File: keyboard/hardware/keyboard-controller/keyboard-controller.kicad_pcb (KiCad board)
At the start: 2 copper layers, 195 x 65 mm, 50 parts, among them J1 Debug_Pins, J2 Barrel_Jack_Switch, J3 Keybed Connector, J5 CV_OUT, J6 GATE_OUT, SW3 OCTAVE_UP, SW4 OCTAVE_DOWN, SW5 FUNC, U1 Pico, U2 MCP4921, U3 L78L09_TO92, U4 TL431, U5 LM1117-3.3, U6 74HC164, U7 74HC164, U8 LM358, U9 LM358

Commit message: Added power polarity symbol to keyboard pcb
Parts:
- added REF**: Polarity_Center_Positive_6mm_SilkScreen, Symbol:Polarity_Center_Positive_6mm_SilkScreen, F.Cu at (136.7, 144.8)
- U2, U8, U9: footprint Package_DIP:DIP-8_W7.62mm_Socket -> Package_DIP:DIP-8_W7.62mm
- U6, U7: footprint Package_DIP:DIP-14_W7.62mm_Socket -> Package_DIP:DIP-14_W7.62mm
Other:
- board text added: "12V"

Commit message: Fixes to keyboard controller rev1
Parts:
- SW3: value OCTAVE_UP -> FUNC
- SW4: value OCTAVE_DOWN -> OCTAVE_UP
- SW5: value FUNC -> OCTAVE_DOWN
- U2, U8, U9: footprint Package_DIP:DIP-8_W7.62mm -> Package_DIP:DIP-8_W7.62mm_Socket
- U6, U7: footprint Package_DIP:DIP-14_W7.62mm -> Package_DIP:DIP-14_W7.62mm_Socket
- moved J3 16.7 mm to (212.6, 180.9), turned to -90 degrees
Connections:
- J3 pad 1: /Key Matrix/MATRIX_C1 -> unconnected-(J3-Pad1)
- J3 pad 10: /MATRIX_R6 -> /Key Matrix/MATRIX_C7
- J3 pad 11: /MATRIX_R5 -> /Key Matrix/MATRIX_C6
- J3 pad 12: /MATRIX_R4 -> /Key Matrix/MATRIX_C5
- J3 pad 13: /MATRIX_R3 -> /Key Matrix/MATRIX_C4
- J3 pad 14: /MATRIX_R2 -> /Key Matrix/MATRIX_C3
- J3 pad 15: /MATRIX_R1 -> /Key Matrix/MATRIX_C2
- J3 pad 16: GND -> /Key Matrix/MATRIX_C1
- J3 pad 2: /Key Matrix/MATRIX_C2 -> /MATRIX_R1
- J3 pad 3: /Key Matrix/MATRIX_C3 -> /MATRIX_R2
- J3 pad 4: /Key Matrix/MATRIX_C4 -> /MATRIX_R3
- J3 pad 5: /Key Matrix/MATRIX_C5 -> /MATRIX_R4
- J3 pad 6: /Key Matrix/MATRIX_C6 -> /MATRIX_R5
- J3 pad 7: /Key Matrix/MATRIX_C7 -> /MATRIX_R6
- J3 pad 8: /Key Matrix/MATRIX_C8 -> /Key Matrix/MATRIX_C9
- J3 pad 9: /Key Matrix/MATRIX_C9 -> /Key Matrix/MATRIX_C8
- U1 pad 13: GND -> unconnected-(U1-Pad13)
- U1 pad 18: GND -> unconnected-(U1-Pad18)
- U1 pad 23: GND -> unconnected-(U1-Pad23)
- U1 pad 28: GND -> unconnected-(U1-Pad28)
- U1 pad 3: GND -> unconnected-(U1-Pad3)
- U1 pad 8: GND -> unconnected-(U1-Pad8)
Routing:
- net /Key Matrix/MATRIX_C4: track 43.9 -> 35.4 mm
- net /Key Matrix/MATRIX_C3: track 35.2 -> 31.6 mm
- net /GATE_OUT: track 51.2 -> 53.7 mm
- net /MATRIX_R1: track 51.5 -> 53.3 mm
- net /Key Matrix/MATRIX_C6: track 26.7 -> 24.9 mm
- net /Key Matrix/MATRIX_C8: track 57.9 -> 56.7 mm
- net /Key Matrix/MATRIX_C7: track 31.3 -> 32.0 mm
- net /Key Matrix/MATRIX_C5: track 25.6 -> 24.9 mm
- net /MATRIX_R6: track 17.8 -> 18.4 mm
- net /Key Matrix/MATRIX_C2: track 28.0 -> 27.4 mm
- net /Key Matrix/MATRIX_C1: track 84.8 -> 84.4 mm, vias 0 -> 1
- net /MATRIX_CLK: track 43.2 -> 43.3 mm, vias 1 -> 0
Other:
- board text added: "TODO: Add more test points"
- board text added: "TODO: Make sure there are no islands in the ground or power planes"
- board text added: "TODO: Probably lower LED resistor values. At least for power LED"
- board text added: "TODO: Update the LM1117 pad to attach the tab to the 3v plane"
- board text added: "TODO: update rev and date"

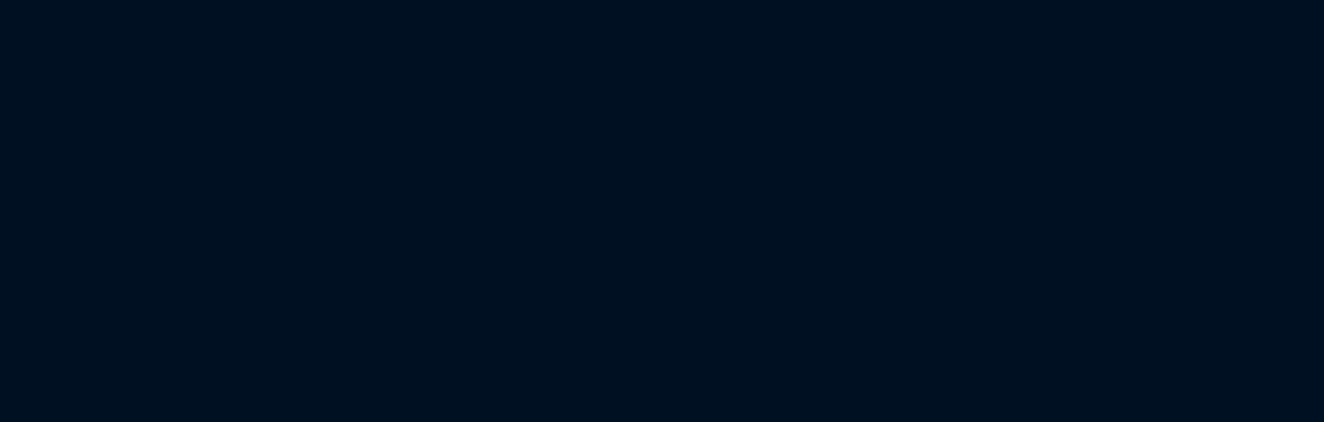
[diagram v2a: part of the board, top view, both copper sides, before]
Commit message: Fixed wiring of keyboard connector, added TODOs
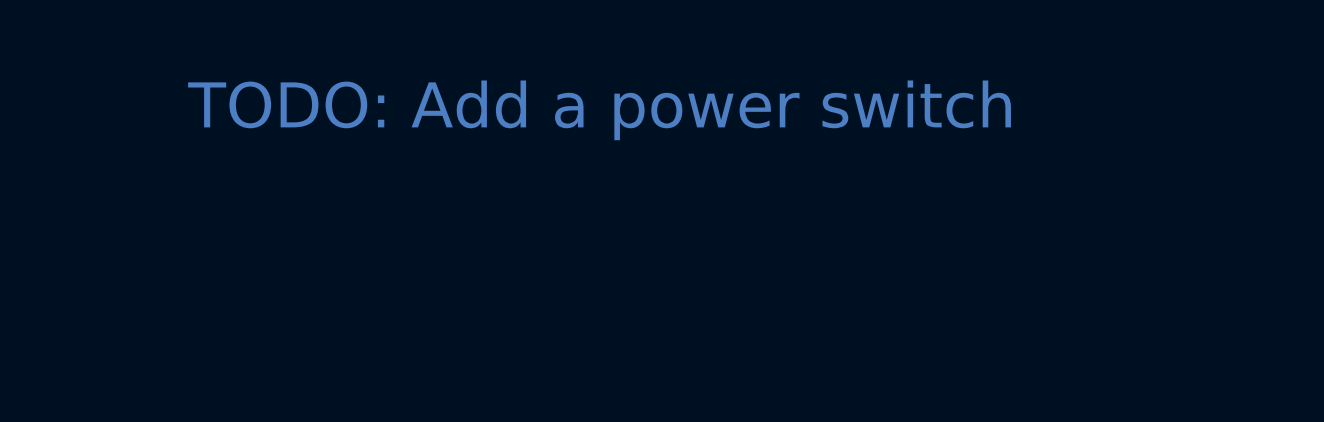
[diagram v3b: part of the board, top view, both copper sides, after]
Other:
- board text added: "TODO: Add a power switch"
- board text added: "TODO: Add more test points for at least ground, power, cv, gate, etc..."
- board text added: "TODO: Fix kicads wiring of the TL431"
- board text removed: "TODO: Add more test points"
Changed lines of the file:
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@@
   (gr_circle (center 284.4 148) (end 285.9 148) (layer "Edge.Cuts") (width 0.2) (fill none))
   (gr_circle (center 270.8 148) (end 272.3 148) (layer "Edge.Cuts") (width 0.2) (fill none))
+  (gr_text "TODO: Add a power switch" (at 117.5 99.5) (layer "B.Cu")
+    (effects (font (size 1.5 1.5) (thickness 0.3)))
+  )
   (gr_text "-O" (at 161.157144 129.1) (layer "F.SilkS")
     (effects (font (size 2.5 2.5) (thickness 0.6)))
@@
     (effects (font (size 1.5 1.5) (thickness 0.3)))
   )
-  (gr_text "TODO: Probably lower LED resistor values. At least for power LED" (at 137.4 98.7) (layer "Cmts.User")
+  (gr_text "TODO: Probably lower LED resistor values. At least for power LED" (at 139.5 102.5) (layer "Cmts.User")
     (effects (font (size 1.5 1.5) (thickness 0.3)))
   )
-  (gr_text "TODO: Add more test points" (at 116.25 105.45) (layer "Cmts.User")
+  (gr_text "TODO: Add more test points for at least ground, power, cv, gate, etc..." (at 143.5 108) (layer "Cmts.User")
     (effects (font (size 1.5 1.5) (thickness 0.3)))
   )
-  (gr_text "TODO: update rev and date" (at 115.75 101.9) (layer "Cmts.User")
+  (gr_text "TODO: update rev and date" (at 117.5 105.5) (layer "Cmts.User")
     (effects (font (size 1.5 1.5) (thickness 0.3)))
   )
-  (gr_text "TODO: Make sure there are no islands in the ground or power planes" (at 140.35 108.25) (layer "Cmts.User")
+  (gr_text "TODO: Fix kicads wiring of the TL431" (at 123.5 96.5) (layer "Cmts.User")
     (effects (font (size 1.5 1.5) (thickness 0.3)))
   )
-  (gr_text "TODO: Update the LM1117 pad to attach the tab to the 3v plane" (at 138.25 111.8) (layer "Cmts.User")
+  (gr_text "TODO: Make sure there are no islands in the ground or power planes" (at 142.5 110.5) (layer "Cmts.User")
+    (effects (font (size 1.5 1.5) (thickness 0.3)))
+  )
+  (gr_text "TODO: Update the LM1117 pad to attach the tab to the 3v plane" (at 140 113) (layer "Cmts.User")
     (effects (font (size 1.5 1.5) (thickness 0.3)))
   )
@@
     (pts (xy 300 125) (xy 300 190))
     (height -13)
-    (gr_text "2.5591 in" (at 311.2 157.5 90) (layer "Dwgs.User")
+    (gr_text "65.0000 mm" (at 311.2 157.5 90) (layer "Dwgs.User")
       (effects (font (size 1.5 1.5) (thickness 0.3)))
     )
@@
     (pts (xy 105 125) (xy 300 125))
     (height -9)
-    (gr_text "7.6772 in" (at 202.5 114.2) (layer "Dwgs.User")
+    (gr_text "195.0000 mm" (at 202.5 114.2) (layer "Dwgs.User")
       (effects (font (size 1.5 1.5) (thickness 0.3)))
     )
@@
     (pts (xy 111 184) (xy 294 184))
     (height 14.5)
-    (gr_text "7.2047 in" (at 202.5 197.35) (layer "Dwgs.User")
+    (gr_text "183.0000 mm" (at 202.5 197.35) (layer "Dwgs.User")
       (effects (font (size 1 1) (thickness 0.15)))
     )
@@
     (pts (xy 111 131) (xy 111 184))
     (height 12.3)
-    (gr_text "2.0866 in" (at 97.55 157.5 90) (layer "Dwgs.User")
+    (gr_text "53.0000 mm" (at 97.55 157.5 90) (layer "Dwgs.User")
       (effects (font (size 1 1) (thickness 0.15)))
     )
@@
     (pts (xy 111 131) (xy 111 125))
     (height -8.9)
-    (gr_text "0.2362 in" (at 100.3 128 90) (layer "Dwgs.User")
+    (gr_text "6.0000 mm" (at 100.3 128 90) (layer "Dwgs.User")
       (effects (font (size 1.5 1.5) (thickness 0.3)))
     )

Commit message: Completed keyboard controller rev2
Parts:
- added SW1: SW_SPDT, Wealth_Metal_Switches:Slide_Switch_SPDT_SS12F44G5, F.Cu at (121.5, 151.5)
- added TP1: CV_PRE, TestPoint:TestPoint_Pad_D1.5mm, F.Cu at (247.5, 139.8)
- added TP2: GND, TestPoint:TestPoint_Pad_D1.5mm, F.Cu at (112.0, 139.0)
- added TP3: +9V, TestPoint:TestPoint_Pad_D1.5mm, F.Cu at (265.2, 134.9)
- added TP4: +12V, TestPoint:TestPoint_Pad_D1.5mm, F.Cu at (129.0, 144.0)
- added TP5: VREF, TestPoint:TestPoint_Pad_D1.5mm, F.Cu at (257.1, 157.5)
- added TP6: 3.3V, TestPoint:TestPoint_Pad_D1.5mm, F.Cu at (139.3, 168.3)
- added TP7: CV, TestPoint:TestPoint_Pad_D1.5mm, F.Cu at (284.4, 134.6)
- added TP8: Gate, TestPoint:TestPoint_Pad_D1.5mm, F.Cu at (270.8, 134.8)
- U5: moved to B.Cu
- moved C5 26.7 mm to (133.3, 172.2), turned to -90 degrees
- moved C6 18.2 mm to (133.3, 166.2)
- moved U5 13.7 mm to (127.7, 167.0), turned to -90 degrees
- moved REF** 0.73 mm to (136.5, 145.5)
- renumbered D6 to D5, D7 to D6, D8 to D7, D9 to D8, J5 to J4, J6 to J5, R18 to R10, R19 to R11, R6 to R5, R12 to R6, R13 to R7, R15 to R8, R16 to R9, SW3 to SW2, SW4 to SW3, SW5 to SW4, U9 to U8, U8 to U9
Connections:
- J2 pad 1: +12V -> Net-(J2-Pad1)
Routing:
- net +12V: track 160.7 -> 179.3 mm
- net Net-(J2-Pad1): track 0.00 -> 13.6 mm
- net VREF: track 11.4 -> 20.3 mm
- net Net-(J4-PadT): track 26.9 -> 35.4 mm
- net Net-(J5-PadT): track 36.1 -> 44.4 mm
- net +3.3V: track 0.00 -> 6.90 mm
- net +9V: track 0.00 -> 5.34 mm
- net /CV_OUT: track 37.8 -> 42.7 mm
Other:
- board text added: "3.3V"
- board text added: "9V"
- board text added: "CV_PRE"
- board text added: "Keyboard Controller - rev2"
- board text added: "Northridge Synth - 1/24"
- board text added: "OFF"
- board text added: "ON"
- board text added: "VREF"
- board text removed: "Keyboard Controller - rev1"
- board text removed: "Northridge Synth - 12/23"
- board text removed: "TODO: Add a power switch"
- board text removed: "TODO: Add more test points for at least ground, power, cv, gate, etc..."
- board text removed: "TODO: Fix kicads wiring of the TL431"
- board text removed: "TODO: Make sure there are no islands in the ground or power planes"
- board text removed: "TODO: Probably lower LED resistor values. At least for power LED"
- board text removed: "TODO: Update the LM1117 pad to attach the tab to the 3v plane"
- board text removed: "TODO: update rev and date"
